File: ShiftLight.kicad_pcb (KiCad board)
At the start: 2 copper layers, 66.3 x 15.2 mm, 58 parts, among them J1 0533980471, J2 0533980571, U1 VOS618A, U2 LMR51406YDBV, U3 MSPM0C1104SDDFR, U4 TLC59208F, U5 VEML7700, U6 TLV803E

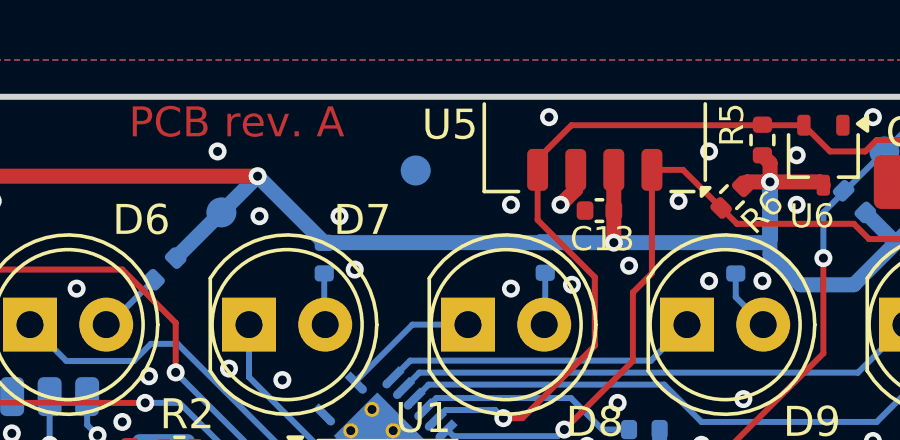
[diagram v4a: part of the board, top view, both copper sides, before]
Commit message: Layout: Update footprints to fix DRC errors
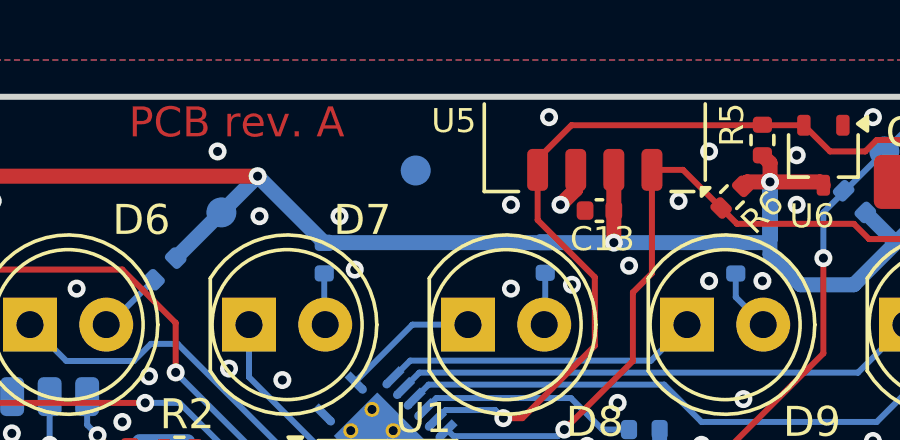
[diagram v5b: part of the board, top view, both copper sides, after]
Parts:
- L1: footprint Inductor_SMD:L_TDK_VLS3015CX -> Personal_Lib:L_TDK_VLS3015CX
- U5: footprint Sensor:Vishay_VEML7700 -> Personal_Lib:Vishay_VEML7700
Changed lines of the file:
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@@
 			(net 3 "GND")
 			(pinfunction "VSS")
-			(pintype "power_out")
+			(pintype "power_in")
 		)
 		(pad "4" smd roundrect
@@
 		)
 	)
-	(footprint "Sensor:Vishay_VEML7700"
+	(footprint "Personal_Lib:Vishay_VEML7700"
 		(layer "F.Cu")
 		(at 115.951 77.917602)
 		(property "Reference" "U5"
-			(at -4.826 -0.828602 0)
+			(at -4.699 -0.955602 0)
 			(layer "F.SilkS")
 			(effects
 				(font
-					(size 1 1)
+					(size 0.8 0.8)
 					(thickness 0.15)
 				)
@@
 		)
 		(property "Value" "VEML7700"
-			(at -2.921 0.441398 90)
+			(at -2.921 1.838398 180)
 			(layer "F.Fab")
 			(effects
@@
 			)
 		)
-		(property "Footprint" "Sensor:Vishay_VEML7700"
+		(property "Footprint" "Personal_Lib:Vishay_VEML7700"
 			(at 0 0 0)
 			(unlocked yes)
@@
 			)
 		)
-		(property ki_fp_filters "Broadcom*LGA*2x2mm*P0.53mm*")
+		(property "MPN" ""
+			(at 0 0 0)
+			(unlocked yes)
+			(layer "F.Fab")
+			(hide yes)
+			(effects
+				(font
+					(size 1 1)
+					(thickness 0.15)
+				)
+			)
+		)
+		(property "No_BOM" ""
+			(at 0 0 0)
+			(unlocked yes)
+			(layer "F.Fab")
+			(hide yes)
+			(effects
+				(font
+					(size 1 1)
+					(thickness 0.15)
+				)
+			)
+		)
 		(sheetname "02_MCU")
 		(sheetfile "02_mcu.kicad_sch")
@@
 			(effects
 				(font
-					(size 0.8 0.8)
-					(thickness 0.12)
+					(size 0.5 0.5)
+					(thickness 0.1)
 				)
 			)
@@
 			(pintype "bidirectional")
 		)
-		(model "W:/_Downloads/veml7700/84592VEML7700.stp"
+		(model "${KIPRJMOD}/libraries/3dmodels/84592VEML7700.stp"
 			(offset
 				(xyz 0 -0.75 1.5)
@@
 		)
 	)
-	(footprint "Inductor_SMD:L_TDK_VLS3015CX"
+	(footprint "Personal_Lib:L_TDK_VLS3015CX"
 		(layer "B.Cu")
 		(at 78.613 86.163 -90)
@@
 		(tags "inductor TDK VLS SMD VLS6045EF VLS6045AF")
 		(property "Reference" "L1"
-			(at 2.864 0 0)
+			(at 2.991 -0.889 0)
 			(unlocked yes)
 			(layer "B.SilkS")
@@
 		)
 		(property "Value" "15u"
-			(at 2.61 -0.508 0)
+			(at 2.61 -0.762 0)
 			(unlocked yes)
 			(layer "B.Fab")
@@
 			)
 		)
-		(property "Footprint" "Inductor_SMD:L_TDK_VLS3015CX"
+		(property "Footprint" "Personal_Lib:L_TDK_VLS3015CX"
 			(at 0 0 90)
 			(unlocked yes)
@@
 		)
 		(property "MPN" "VLS3015CX-150M-H"
-			(at 0 0 90)
+			(at 0 0 -90)
 			(unlocked yes)
 			(layer "B.Fab")
@@
 		)
 		(property "No_BOM" ""
-			(at 0 0 90)
+			(at 0 0 -90)
 			(unlocked yes)
 			(layer "B.Fab")
@@
 			(layer "B.SilkS")
 		)
-		(fp_poly
-			(pts
-				(xy -2.286 1.726) (xy 2.282 1.726) (xy 2.282 -1.726) (xy -2.286 -1.726)
-			)
+		(fp_rect
+			(start -2.286 1.726)
+			(end 2.282 -1.726)
 			(stroke
 				(width 0.05)
@@
 			(layer "B.CrtYd")
 		)
-		(fp_poly
-			(pts
-				(xy -2.0475 1.524) (xy 2.032 1.524) (xy 2.032 -1.524) (xy -2.0475 -1.524)
-			)
+		(fp_rect
+			(start -2.0475 1.524)
+			(end 2.032 -1.524)
 			(stroke
 				(width 0.1)
@@
 		)
 		(fp_text user "${REFERENCE}"
-			(at 0 0 90)
+			(at 0 0 0)
 			(unlocked yes)
 			(layer "B.Fab")
 			(effects
 				(font
-					(size 1 1)
-					(thickness 0.15)
+					(size 0.8 0.8)
+					(thickness 0.12)
 				)
 				(justify mirror)
@@
 			(net 3 "GND")
 			(pinfunction "GND")
-			(pintype "power_out")
+			(pintype "power_in")
 			(solder_paste_margin -0.025)
 			(zone_connect 2)
@@
 			(net 3 "GND")
 			(pinfunction "EP")
-			(pintype "power_out")
+			(pintype "power_in")
 		)
 		(pad "25" thru_hole circle
@@
 			(net 3 "GND")
 			(pinfunction "EP")
-			(pintype "power_out")
+			(pintype "power_in")
 			(zone_connect 2)
 		)
@@
 			(net 3 "GND")
 			(pinfunction "EP")
-			(pintype "power_out")
+			(pintype "power_in")
 			(zone_connect 2)
 		)
@@
 			(net 3 "GND")
 			(pinfunction "EP")
-			(pintype "power_out")
+			(pintype "power_in")
 			(zone_connect 2)
 		)
@@
 			(net 3 "GND")
 			(pinfunction "EP")
-			(pintype "power_out")
+			(pintype "power_in")
 			(zone_connect 2)
 		)
@@
 			(net 3 "GND")
 			(pinfunction "EP")
-			(pintype "power_out")
+			(pintype "power_in")
 			(zone_connect 2)
 		)
@@
 			(net 3 "GND")
 			(pinfunction "EP")
-			(pintype "power_out")
+			(pintype "power_in")
 			(zone_connect 2)
 		)

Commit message: Layout: Minor improvements
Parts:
- moved R9 0.99 mm to (117.0, 88.0), turned to 135 degrees
- moved D12 0.07 mm to (140.2, 84.2)
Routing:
- net 3V3: track 130.0 -> 128.7 mm
- net GND: vias 81 -> 83
